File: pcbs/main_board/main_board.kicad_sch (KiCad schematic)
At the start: 5 parts, among them J3 LED strip, J4 Motor, U1 mini_esp32

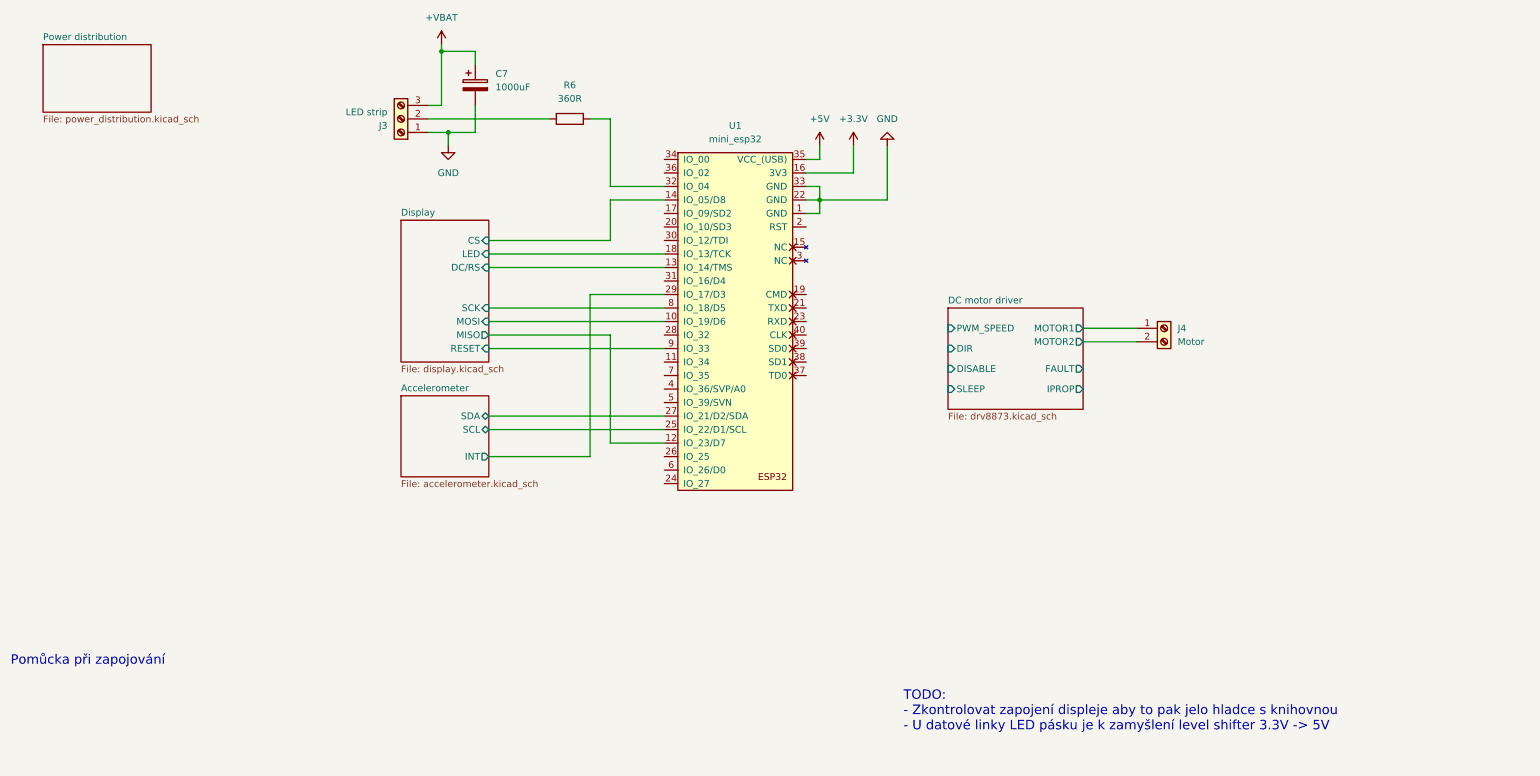
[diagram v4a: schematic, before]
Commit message: wire m driver to esp
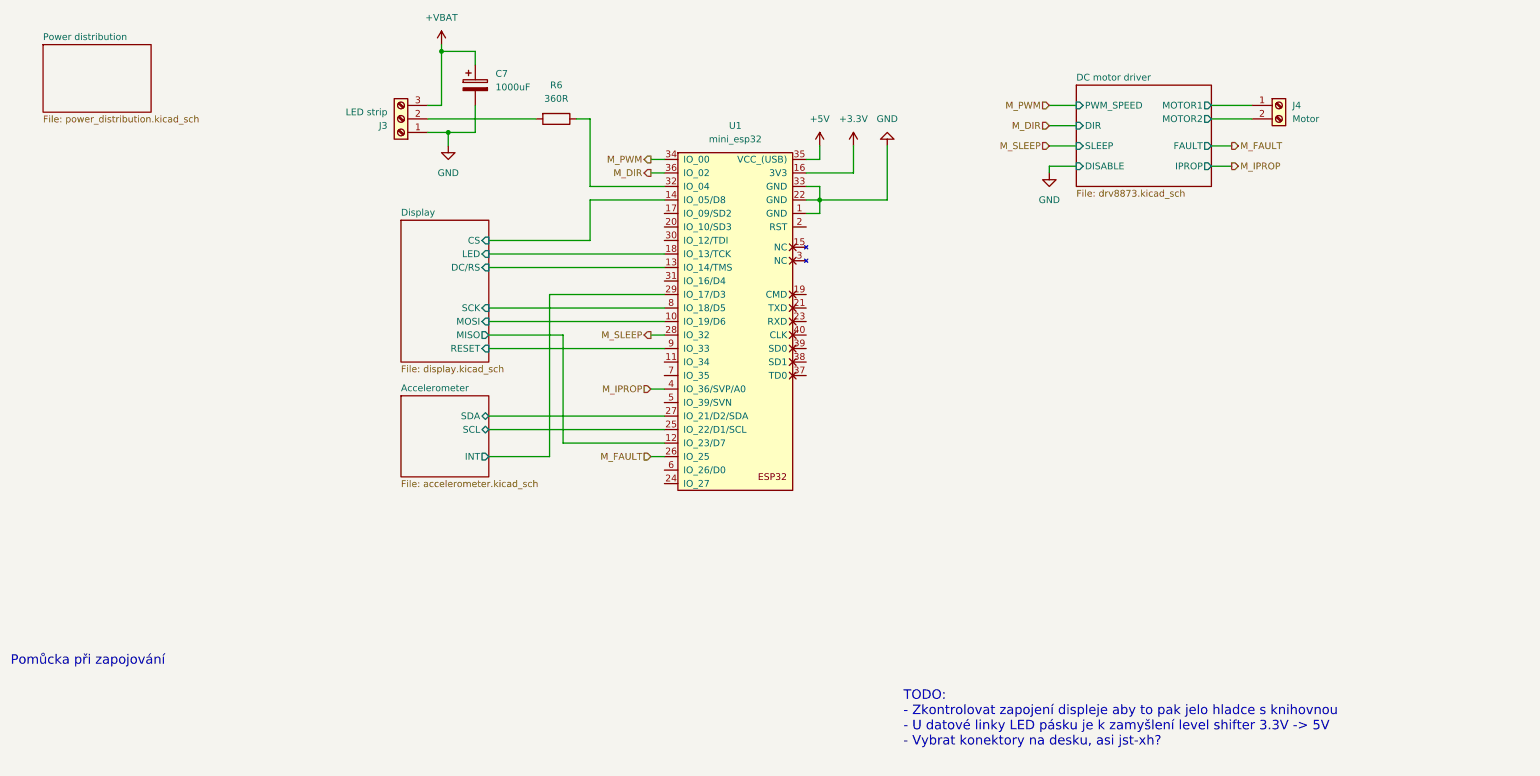
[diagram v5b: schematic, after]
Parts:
- C7: footprint (none) -> Capacitor_Tantalum_SMD:CP_EIA-7360-38_Kemet-E_HandSolder; Manufacturer Part Number (none) -> TCN4108M006R0055; Supplier (none) -> Mouser; Supplier Part Number (none) -> 581-TCN4108M006R0055
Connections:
- net M_FAULT: now reaches U1.26 (IO_25)
- net M_SLEEP: now reaches U1.28 (IO_32)
- net M_PWM: now reaches U1.34 (IO_00)
- net M_DIR: now reaches U1.36 (IO_02)
- net M_IPROP: now reaches U1.4 (IO_36/SVP/A0)
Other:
- note added: "TODO: - Zkontrolovat zapojení displeje aby to pak jelo hladce s knihovnou - U datové linky LED pásku je k zamyšlení level shifter 3.3V -> 5V - Vybrat konektory na desku, asi jst-xh?"
- note removed: "TODO: - Zkontrolovat zapojení displeje aby to pak jelo hladce s knihovnou - U datové linky LED pásku je k zamyšlení level shifter 3.3V -> 5V"
- moved on the sheet: J4, R6

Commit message: Add ideal diode
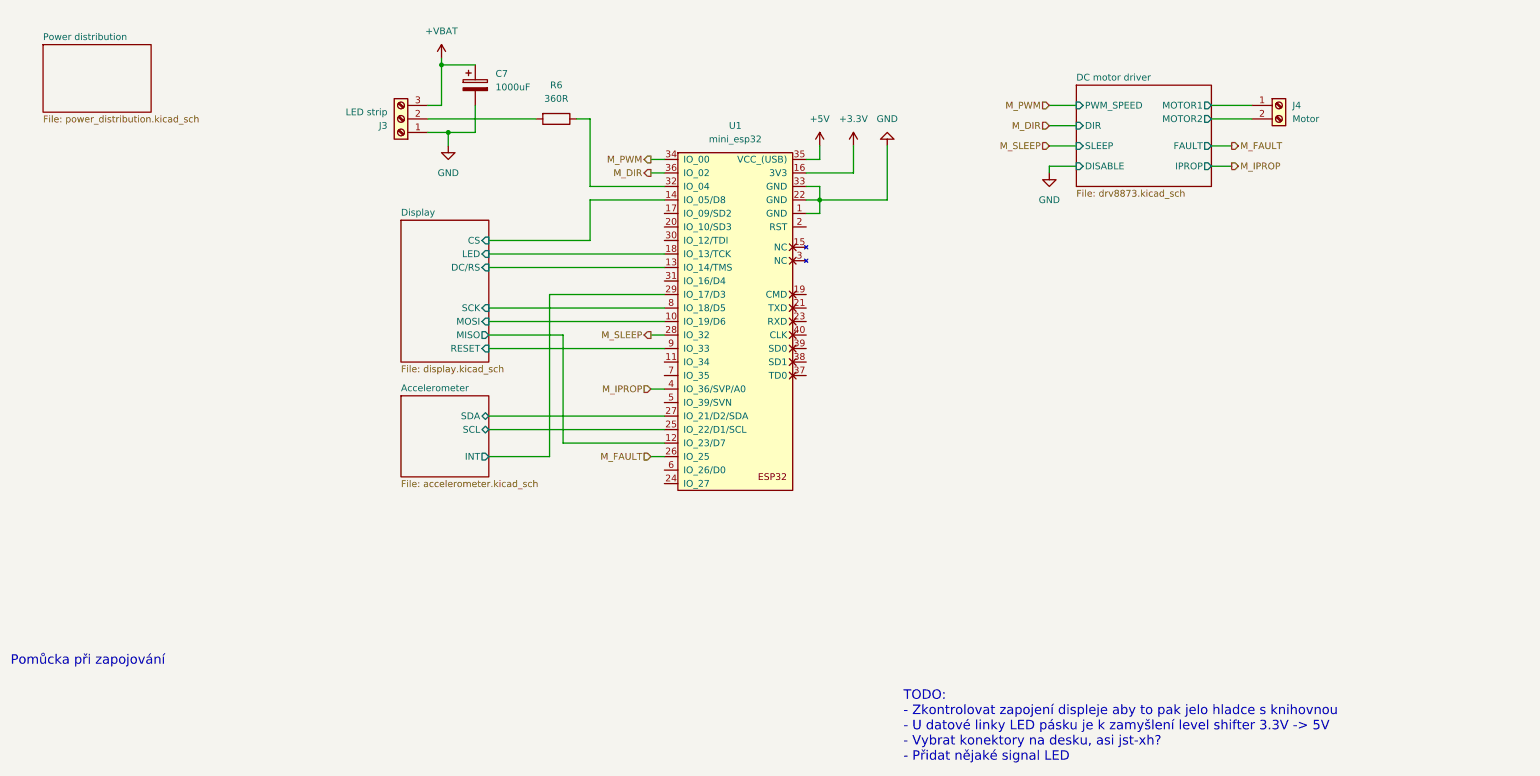
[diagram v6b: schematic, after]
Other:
- note added: "TODO: - Zkontrolovat zapojení displeje aby to pak jelo hladce s knihovnou - U datové linky LED pásku je k zamyšlení level shifter 3.3V -> 5V - Vybrat konektory na desku, asi jst-xh? - Přidat nějaké signal LED"
- note removed: "TODO: - Zkontrolovat zapojení displeje aby to pak jelo hladce s knihovnou - U datové linky LED pásku je k zamyšlení level shifter 3.3V -> 5V - Vybrat konektory na desku, asi jst-xh?"
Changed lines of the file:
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@@
 	(generator_version "9.0")
 	(paper "A4")
-	(text "TODO:\n- Zkontrolovat zapojení displeje aby to pak jelo hladce s knihovnou\n- U datové linky LED pásku je k zamyšlení level shifter 3.3V -> 5V\n- Vybrat konektory na desku, asi jst-xh?\n"
+	(text "TODO:\n- Zkontrolovat zapojení displeje aby to pak jelo hladce s knihovnou\n- U datové linky LED pásku je k zamyšlení level shifter 3.3V -> 5V\n- Vybrat konektory na desku, asi jst-xh?\n- Přidat nějaké signal LED\n"
 		(exclude_from_sim no)
 		(at 180.848 141.732 0)
@@
 	)
 	(junction
-		(at 165.1 49.53)
+		(at 93.98 24.13)
 		(diameter 0)
 		(color 0 0 0 0)
 	)
 	(junction
-		(at 93.98 21.59)
+		(at 165.1 49.53)
 		(diameter 0)
 		(color 0 0 0 0)
@@
 	(wire
 		(pts
+			(xy 93.98 22.86) (xy 93.98 24.13)
+		)
+		(stroke
+			(width 0)
+			(type default)
+		)
+	)
+	(wire
+		(pts
 			(xy 119.38 34.29) (xy 121.92 34.29)
 		)
@@
 	(wire
 		(pts
+			(xy 93.98 24.13) (xy 93.98 31.75)
+		)
+		(stroke
+			(width 0)
+			(type default)
+		)
+	)
+	(wire
+		(pts
 			(xy 208.28 35.56) (xy 213.36 35.56)
 		)
@@
 	(wire
 		(pts
-			(xy 100.33 21.59) (xy 93.98 21.59)
+			(xy 100.33 24.13) (xy 93.98 24.13)
 		)
 		(stroke
@@
 	(wire
 		(pts
-			(xy 93.98 21.59) (xy 93.98 31.75)
-		)
-		(stroke
-			(width 0)
-			(type default)
-		)
-	)
-	(wire
-		(pts
 			(xy 102.87 74.93) (xy 116.84 74.93)
 		)
@@
 	(wire
 		(pts
-			(xy 93.98 20.32) (xy 93.98 21.59)
-		)
-		(stroke
-			(width 0)
-			(type default)
-		)
-	)
-	(wire
-		(pts
 			(xy 95.25 39.37) (xy 95.25 36.83)
 		)
@@
 	(wire
 		(pts
-			(xy 100.33 24.13) (xy 100.33 21.59)
-		)
-		(stroke
-			(width 0)
-			(type default)
-		)
-	)
-	(wire
-		(pts
 			(xy 121.92 57.15) (xy 121.92 49.53)
 		)
@@
 	(symbol
 		(lib_id "power:VCC")
-		(at 93.98 20.32 0)
+		(at 93.98 22.86 0)
 		(unit 1)
 		(exclude_from_sim no)
@@
 		(fields_autoplaced yes)
 		(property "Reference" "#PWR030"
-			(at 93.98 24.13 0)
+			(at 93.98 26.67 0)
 			(effects
 				(font
@@
 		)
 		(property "Value" "+VBAT"
-			(at 93.98 15.24 0)
+			(at 93.98 17.78 0)
 			(effects
 				(font
@@
 		)
 		(property "Footprint" ""
-			(at 93.98 20.32 0)
+			(at 93.98 22.86 0)
 			(effects
 				(font
@@
 		)
 		(property "Datasheet" ""
-			(at 93.98 20.32 0)
+			(at 93.98 22.86 0)
 			(effects
 				(font
@@
 		)
 		(property "Description" "Power symbol creates a global label with name \"VCC\""
-			(at 93.98 20.32 0)
+			(at 93.98 22.86 0)
 			(effects
 				(font

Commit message: Add reverse polarity protection
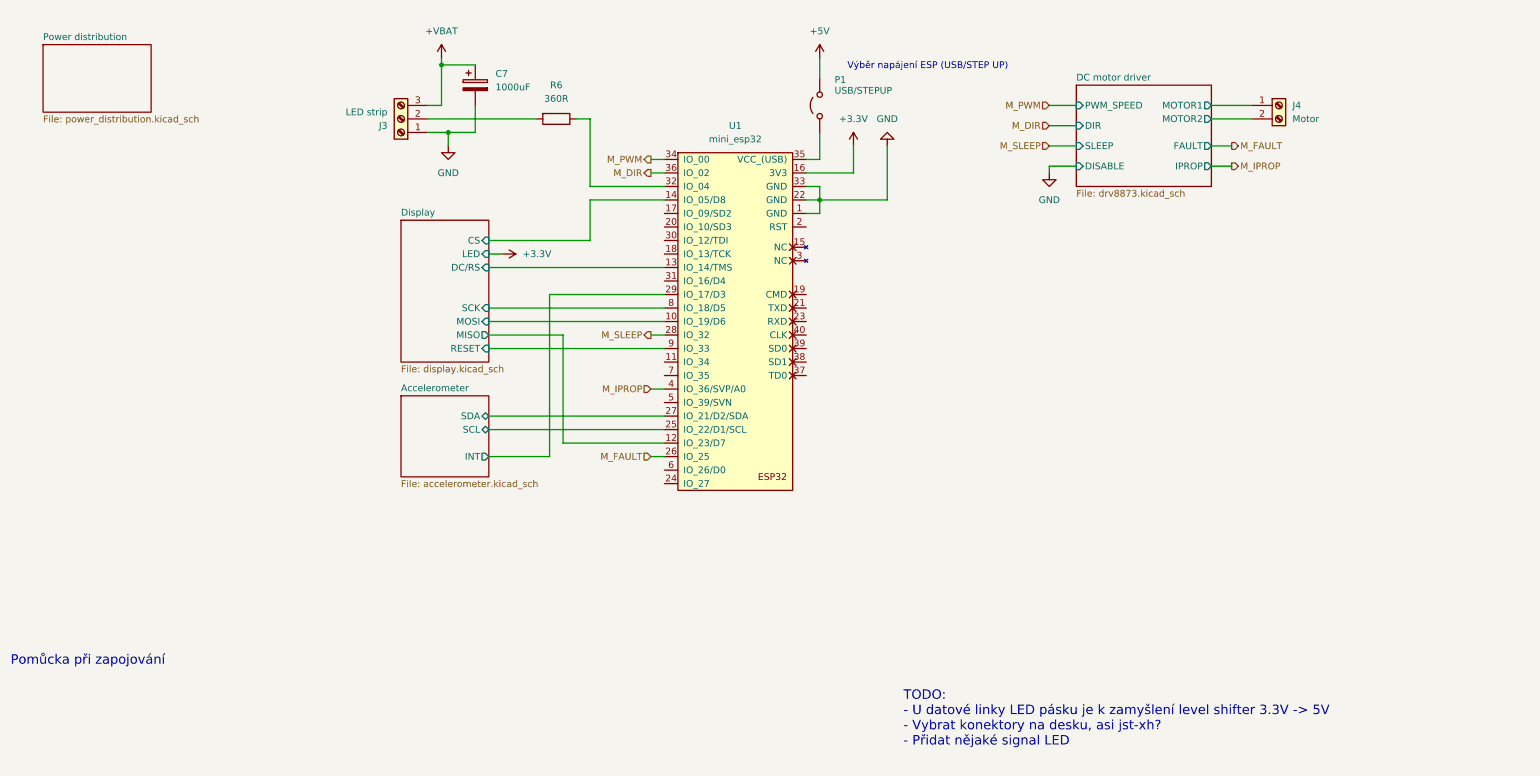
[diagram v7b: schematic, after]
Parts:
- added P1: USB/STEPUP, Connector_PinHeader_2.54mm:PinHeader_1x03_P2.54mm_Vertical, symbol Jumper:Jumper_2_Open
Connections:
- net +5V: now also P1.2 (B); no longer U1.35 (VCC_(USB))
- net Display/LED: no longer names the net of U1.18 (IO_13/TCK)
- new net: P1.1 (A), U1.35 (VCC_(USB))
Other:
- note added: "TODO: - U datové linky LED pásku je k zamyšlení level shifter 3.3V -> 5V - Vybrat konektory na desku, asi jst-xh? - Přidat nějaké signal LED"
- note added: "Výběr napájení ESP (USB/STEP UP)"
- note removed: "TODO: - Zkontrolovat zapojení displeje aby to pak jelo hladce s knihovnou - U datové linky LED pásku je k zamyšlení level shifter 3.3V -> 5V - Vybrat konektory na desku, asi jst-xh? - Přidat nějaké signal LED"
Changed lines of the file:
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@@
 	(generator_version "9.0")
 	(paper "A4")
-	(text "TODO:\n- Zkontrolovat zapojení displeje aby to pak jelo hladce s knihovnou\n- U datové linky LED pásku je k zamyšlení level shifter 3.3V -> 5V\n- Vybrat konektory na desku, asi jst-xh?\n- Přidat nějaké signal LED\n"
+	(text "TODO:\n- U datové linky LED pásku je k zamyšlení level shifter 3.3V -> 5V\n- Vybrat konektory na desku, asi jst-xh?\n- Přidat nějaké signal LED\n"
 		(exclude_from_sim no)
 		(at 180.848 141.732 0)
@@
 		)
 	)
+	(text "Výběr napájení ESP (USB/STEP UP)"
+		(exclude_from_sim no)
+		(at 185.42 24.384 0)
+		(effects
+			(font
+				(size 1.27 1.27)
+			)
+		)
+	)
 	(text "Pomůcka při zapojování"
 		(exclude_from_sim no)
@@
 	(wire
 		(pts
+			(xy 165.1 22.86) (xy 165.1 26.67)
+		)
+		(stroke
+			(width 0)
+			(type default)
+		)
+	)
+	(wire
+		(pts
 			(xy 165.1 41.91) (xy 162.56 41.91)
 		)
@@
 	(wire
 		(pts
-			(xy 102.87 59.69) (xy 135.89 59.69)
-		)
-		(stroke
-			(width 0)
-			(type default)
-		)
-	)
-	(wire
-		(pts
 			(xy 93.98 31.75) (xy 91.44 31.75)
 		)
@@
 	(wire
 		(pts
-			(xy 165.1 39.37) (xy 165.1 41.91)
+			(xy 102.87 59.69) (xy 105.41 59.69)
 		)
 		(stroke
@@
 	(wire
 		(pts
+			(xy 165.1 36.83) (xy 165.1 41.91)
+		)
+		(stroke
+			(width 0)
+			(type default)
+		)
+	)
+	(wire
+		(pts
 			(xy 208.28 31.75) (xy 213.36 31.75)
 		)
@@
 	)
 	(symbol
+		(lib_id "Jumper:Jumper_2_Open")
+		(at 165.1 31.75 90)
+		(unit 1)
+		(exclude_from_sim no)
+		(in_bom yes)
+		(on_board yes)
+		(dnp no)
+		(property "Reference" "P1"
+			(at 167.894 26.924 90)
+			(effects
+				(font
+					(size 1.27 1.27)
+				)
+				(justify right)
+			)
+		)
+		(property "Value" "USB/STEPUP"
+			(at 167.894 28.956 90)
+			(effects
+				(font
+					(size 1.27 1.27)
+				)
+				(justify right)
+			)
+		)
+		(property "Footprint" "Connector_PinHeader_2.54mm:PinHeader_1x03_P2.54mm_Vertical"
+			(at 165.1 31.75 0)
+			(effects
+				(font
+					(size 1.27 1.27)
+				)
+				(hide yes)
+			)
+		)
+		(property "Datasheet" "~"
+			(at 165.1 31.75 0)
+			(effects
+				(font
+					(size 1.27 1.27)
+				)
+				(hide yes)
+			)
+		)
+		(property "Description" "Jumper"
+			(at 165.1 31.75 0)
+			(effects
+				(font
+					(size 1.27 1.27)
+				)
+				(hide yes)
+			)
+		)
+		(pin "2"
+		)
+		(pin "1"
+		)
+		(instances
+			(project "main_board"
+				(path "/86b00c07-962a-4c6d-8d05-813891e412c9"
+					(reference "P1")
+					(unit 1)
+				)
+			)
+		)
+	)
+	(symbol
 		(lib_id "Connector:Screw_Terminal_01x02")
 		(at 251.46 31.75 0)
@@
 	)
 	(symbol
+		(lib_id "power:VCC")
+		(at 105.41 59.69 270)
+		(unit 1)
+		(exclude_from_sim no)
+		(in_bom yes)
+		(on_board yes)
+		(dnp no)
+		(fields_autoplaced yes)
+		(property "Reference" "#PWR035"
+			(at 101.6 59.69 0)
+			(effects
+				(font
+					(size 1.27 1.27)
+				)
+				(hide yes)
+			)
+		)
+		(property "Value" "+3.3V"
+			(at 109.22 59.6899 90)
+			(effects
+				(font
+					(size 1.27 1.27)
+				)
+				(justify left)
+			)
+		)
+		(property "Footprint" ""
+			(at 105.41 59.69 0)
+			(effects
+				(font
+					(size 1.27 1.27)
+				)
+				(hide yes)
+			)
+		)
+		(property "Datasheet" ""
+			(at 105.41 59.69 0)
+			(effects
+				(font
+					(size 1.27 1.27)
+				)
+				(hide yes)
+			)
+		)
+		(property "Description" "Power symbol creates a global label with name \"VCC\""
+			(at 105.41 59.69 0)
+			(effects
+				(font
+					(size 1.27 1.27)
+				)
+				(hide yes)
+			)
+		)
+		(pin "1"
+		)
+		(instances
+			(project "main_board"
+				(path "/86b00c07-962a-4c6d-8d05-813891e412c9"
+					(reference "#PWR035")
+					(unit 1)
+				)
+			)
+		)
+	)
+	(symbol
 		(lib_id "power:GND")
 		(at 177.8 39.37 180)
@@
 	(symbol
 		(lib_id "power:VCC")
-		(at 165.1 39.37 0)
+		(at 165.1 22.86 0)
 		(unit 1)
 		(exclude_from_sim no)
@@
 		(fields_autoplaced yes)
 		(property "Reference" "#PWR021"
-			(at 165.1 43.18 0)
+			(at 165.1 26.67 0)
 			(effects
 				(font
@@
 		)
 		(property "Value" "+5V"
-			(at 165.1 34.29 0)
+			(at 165.1 17.78 0)
 			(effects
 				(font
@@
 		)
 		(property "Footprint" ""
-			(at 165.1 39.37 0)
+			(at 165.1 22.86 0)
 			(effects
 				(font
@@
 		)
 		(property "Datasheet" ""
-			(at 165.1 39.37 0)
+			(at 165.1 22.86 0)
 			(effects
 				(font
@@
 		)
 		(property "Description" "Power symbol creates a global label with name \"VCC\""
-			(at 165.1 39.37 0)
+			(at 165.1 22.86 0)
 			(effects
 				(font
